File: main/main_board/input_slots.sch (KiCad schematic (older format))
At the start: 26 parts, among them J3 DEBUG, J7 SCKB, J8 SCKA, M1 microzed, U14 74LVC541A, U15 FIN1047, U16 FIN1047, U17 FIN1047, U5 DS90LV048, X1 microzed

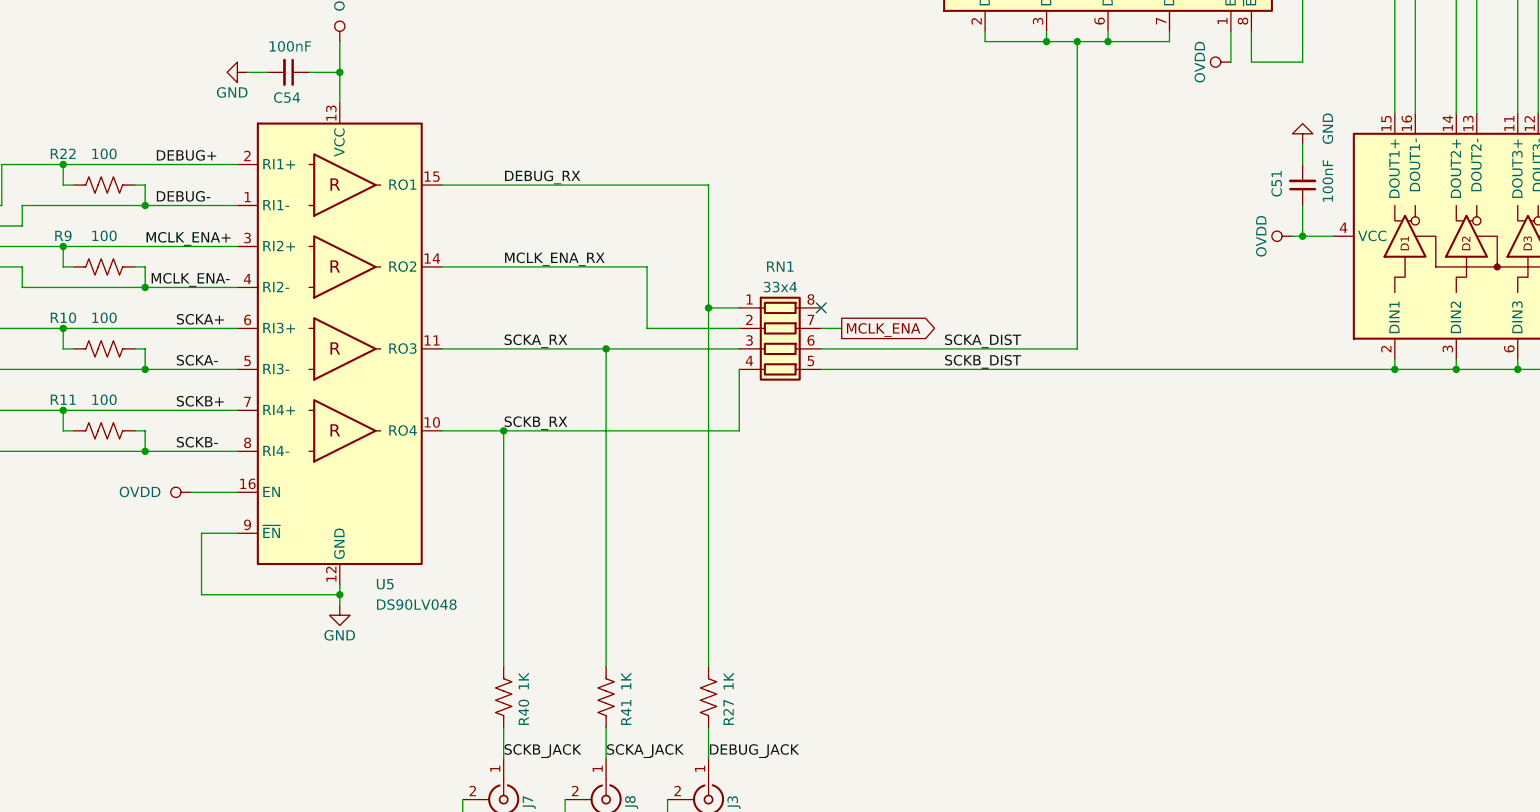
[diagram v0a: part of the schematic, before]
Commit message: Main board is now fully routed and passing DRC. Minor changes related to pin remapping. I2C and one-wire pullups are to OVDD 3.3V, not VCCIO 2.5V. Changes to supply decoupling and VREF- net in reference.sch, suggested by routing.
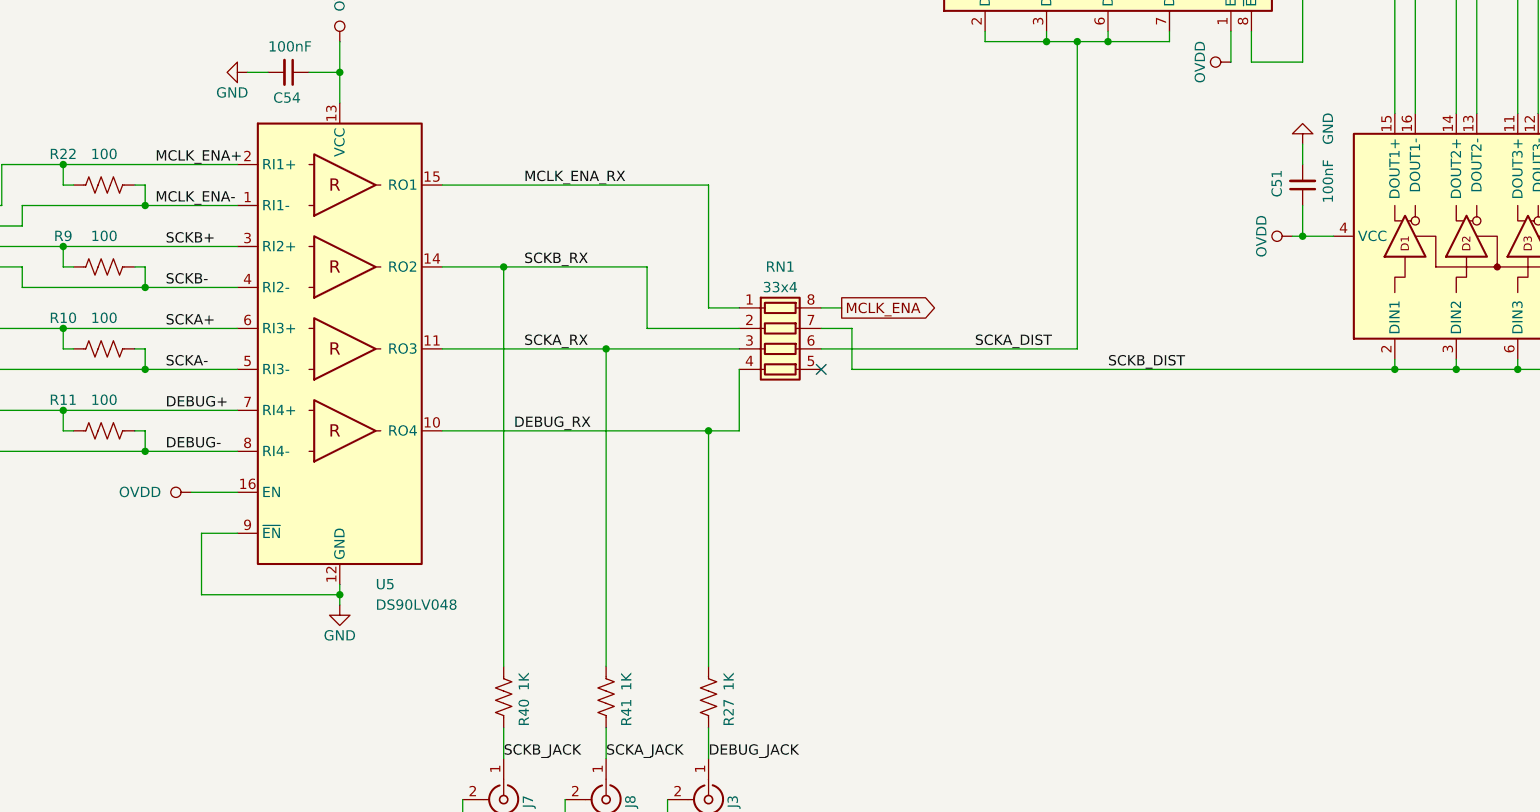
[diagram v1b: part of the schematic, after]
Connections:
- wire segments 333 -> 336
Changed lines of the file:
@@
 	8300 11950 8300 11650
 Wire Wire Line
-	8300 11650 7300 11650
+	8300 11650 7600 11650
 Wire Wire Line
 	8600 11850 8600 11250
 Wire Wire Line
 	8600 11250 7300 11250
-Text GLabel 9250 11950 2    50   Output ~ 0
+Text GLabel 9250 11850 2    50   Output ~ 0
 MCLK_ENA
 Wire Wire Line
-	9250 11950 9150 11950
-Wire Wire Line
-	7600 13600 7600 12450
+	9250 11850 9150 11850
 Wire Wire Line
 	8100 13600 8100 12050
@@
 Wire Wire Line
 	10400 10550 10400 12050
-Wire Wire Line
-	9150 12050 10400 12050
-Wire Wire Line
-	9150 12150 11950 12150
-Connection ~ 11950 12150
 Wire Wire Line
 	4400 11550 5450 11550
@@
 Wire Wire Line
 	2600 11550 2700 11550
-NoConn ~ 9150 11850
 NoConn ~ 6650 6300
 Wire Wire Line
@@
 Wire Wire Line
 	8900 8000 15850 8000
-Text Label 5850 11550 0    50   ~ 0
-MCLK_ENA+
-Text Label 5875 11750 0    50   ~ 0
-MCLK_ENA-
-Text Label 6000 11950 0    50   ~ 0
-SCKA+
-Text Label 6000 12150 0    50   ~ 0
-SCKA-
-Text Label 6000 12350 0    50   ~ 0
-SCKB+
-Text Label 6000 12550 0    50   ~ 0
-SCKB-
-Text Label 9750 12050 0    50   ~ 0
+Text Label 9900 12050 0    50   ~ 0
 SCKA_DIST
-Text Label 9750 12150 0    50   ~ 0
-SCKB_DIST
 $Comp
 L microzed:microzed M1
@@
 Wire Wire Line
 	5500 8500 5500 8600
-Text Label 7600 12050 0    50   ~ 0
+Text Label 7700 12050 0    50   ~ 0
 SCKA_RX
-Text Label 7600 12450 0    50   ~ 0
+Text Label 7700 11650 0    50   ~ 0
 SCKB_RX
-Text Label 7600 11650 0    50   ~ 0
+Text Label 7700 11250 0    50   ~ 0
 MCLK_ENA_RX
-Text Label 7600 11250 0    50   ~ 0
+Text Label 7650 12450 0    50   ~ 0
 DEBUG_RX
 Wire Wire Line
@@
 Wire Wire Line
 	8300 11950 8750 11950
-Wire Wire Line
-	7600 12450 7300 12450
 Connection ~ 8100 12050
 Wire Wire Line
-	8100 12050 7300 12050
-Connection ~ 8600 11850
-Wire Wire Line
 	8100 12050 8750 12050
 Wire Wire Line
 	8600 11850 8750 11850
 Wire Wire Line
-	8600 11850 8600 13600
-Wire Wire Line
-	7600 12450 8750 12450
-Wire Wire Line
 	8750 12450 8750 12150
-Connection ~ 7600 12450
-Text Label 5900 11150 0    50   ~ 0
-DEBUG+
-Text Label 5900 11350 0    50   ~ 0
-DEBUG-
 Wire Wire Line
 	5250 11350 5850 11350
-Connection ~ 5450 11550
-Connection ~ 5850 11750
-Wire Wire Line
-	5450 11550 6300 11550
-Wire Wire Line
-	5850 11750 6300 11750
-Connection ~ 5450 11950
-Connection ~ 5850 12150
-Wire Wire Line
-	5450 11950 6300 11950
-Wire Wire Line
-	5850 12150 6300 12150
-Connection ~ 5450 12350
-Connection ~ 5850 12550
-Wire Wire Line
-	5450 12350 6300 12350
-Wire Wire Line
-	5850 12550 6300 12550
 Wire Wire Line
 	4400 11150 4550 11150
@@
 Wire Wire Line
 	5850 11250 5850 11350
-Connection ~ 5450 11150
-Wire Wire Line
-	5450 11150 6300 11150
-Connection ~ 5850 11350
-Wire Wire Line
-	5850 11350 6300 11350
 Text GLabel 15700 3550 0    50   Input ~ 0
 IN1_CARDSEL
@@
 Wire Wire Line
 	8900 8000 8900 8300
+Connection ~ 5850 11350
+Wire Wire Line
+	5850 11350 6300 11350
+Connection ~ 5450 11150
+Wire Wire Line
+	5450 11150 6300 11150
+Connection ~ 5850 12550
+Wire Wire Line
+	5850 12550 6300 12550
+Connection ~ 5450 12350
+Wire Wire Line
+	5450 12350 6300 12350
+Connection ~ 5850 12150
+Wire Wire Line
+	5850 12150 6300 12150
+Connection ~ 5450 11950
+Wire Wire Line
+	5450 11950 6300 11950
+Connection ~ 5850 11750
+Wire Wire Line
+	5850 11750 6300 11750
+Connection ~ 5450 11550
+Wire Wire Line
+	5450 11550 6300 11550
+Text Label 5950 12350 0    50   ~ 0
+DEBUG+
+Text Label 5950 12550 0    50   ~ 0
+DEBUG-
+Text Label 5950 11950 0    50   ~ 0
+SCKA+
+Text Label 5950 12150 0    50   ~ 0
+SCKA-
+Text Label 5950 11550 0    50   ~ 0
+SCKB+
+Text Label 5950 11750 0    50   ~ 0
+SCKB-
+Text Label 5900 11150 0    50   ~ 0
+MCLK_ENA+
+Text Label 5900 11350 0    50   ~ 0
+MCLK_ENA-
+Wire Wire Line
+	8600 13600 8600 12450
+Wire Wire Line
+	7300 12450 8600 12450
+Connection ~ 8600 12450
+Wire Wire Line
+	8600 12450 8750 12450
+Connection ~ 7600 11650
+Wire Wire Line
+	7600 11650 7300 11650
+Wire Wire Line
+	7300 12050 8100 12050
+Wire Wire Line
+	7600 11650 7600 13600
+Text Label 10550 12150 0    50   ~ 0
+SCKB_DIST
+Wire Wire Line
+	9300 12150 11950 12150
+Connection ~ 11950 12150
+Wire Wire Line
+	9300 11950 9300 12150
+Wire Wire Line
+	9150 11950 9300 11950
+Wire Wire Line
+	9150 12050 10400 12050
+NoConn ~ 9150 12150
 $EndSCHEMATC

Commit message: Added testpoints, debug IO port, LEDs, and clock output jack.
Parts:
- removed M1: microzed, main_board:Microzed, symbol microzed:microzed
- removed unit 3 of X1
- added M1: microzed, main_board:Microzed, symbol microzed:microzed
- J3, J7, J8: DK line (none) -> 35
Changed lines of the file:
@@
 F 2 "Connector_Coaxial:MMCX_Molex_73415-1471_Vertical" H 8100 14250 50  0001 C CNN
 F 3 "https://www.molex.com/pdm_docs/sd/734151471_sd.pdf" H 8100 14250 50  0001 C CNN
-F 4 "" H 8100 14250 50  0001 C CNN "DK line"
+F 4 "35" H 8100 14250 50  0001 C CNN "DK line"
 F 5 "CONN MMCX JACK STR 50 OHM PCB" H 8100 14250 50  0001 C CNN "Description"
 F 6 "WM5557-ND" H 8100 14250 50  0001 C CNN "Digikey"
@@
 F 2 "Connector_Coaxial:MMCX_Molex_73415-1471_Vertical" H 7600 14250 50  0001 C CNN
 F 3 "https://www.molex.com/pdm_docs/sd/734151471_sd.pdf" H 7600 14250 50  0001 C CNN
-F 4 "" H 7600 14250 50  0001 C CNN "DK line"
+F 4 "35" H 7600 14250 50  0001 C CNN "DK line"
 F 5 "CONN MMCX JACK STR 50 OHM PCB" H 7600 14250 50  0001 C CNN "Description"
 F 6 "WM5557-ND" H 7600 14250 50  0001 C CNN "Digikey"
@@
 Wire Wire Line
 	4600 12550 5850 12550
+Wire Wire Line
+	17000 1850 17800 1850
+Wire Wire Line
+	17800 1850 17800 1950
+Wire Wire Line
+	17000 1950 17700 1950
+Wire Wire Line
+	17700 1950 17700 2050
+Wire Wire Line
+	17700 2050 17800 2050
+Wire Wire Line
+	17000 2100 17650 2100
+Wire Wire Line
+	17650 2100 17650 2150
+Wire Wire Line
+	17650 2150 17800 2150
+Wire Wire Line
+	17000 2200 17600 2200
+Wire Wire Line
+	17600 2200 17600 2250
+Wire Wire Line
+	17600 2250 17800 2250
+Wire Wire Line
+	17000 2350 17800 2350
+Wire Wire Line
+	17000 2450 17800 2450
+Wire Wire Line
+	17000 2600 17600 2600
+Wire Wire Line
+	17600 2600 17600 2550
+Wire Wire Line
+	17600 2550 17800 2550
+Wire Wire Line
+	17000 2700 17700 2700
+Wire Wire Line
+	17700 2700 17700 2650
+Wire Wire Line
+	17700 2650 17800 2650
 $Comp
 L microzed:microzed X1
-U 3 1 5F0A97DA
-P 17800 1950
-AR Path="/5F0A97DA" Ref="X1"  Part="2"
-AR Path="/5E525FFE/5F0A97DA" Ref="M1"  Part="3"
-F 0 "M1" H 18000 2200 60  0000 L CNN
-F 1 "microzed" H 18000 2100 60  0000 L CNN
-F 2 "main_board:Microzed" H 18000 2000 60  0001 L CNN
-F 3 "" H 18000 1800 60  0001 L CNN
-	3    17800 1950
-	1    0    0    -1
-$EndComp
-Wire Wire Line
-	17000 1850 17800 1850
-Wire Wire Line
-	17800 1850 17800 1950
-Wire Wire Line
-	17000 1950 17700 1950
-Wire Wire Line
-	17700 1950 17700 2050
-Wire Wire Line
-	17700 2050 17800 2050
-Wire Wire Line
-	17000 2100 17650 2100
-Wire Wire Line
-	17650 2100 17650 2150
-Wire Wire Line
-	17650 2150 17800 2150
-Wire Wire Line
-	17000 2200 17600 2200
-Wire Wire Line
-	17600 2200 17600 2250
-Wire Wire Line
-	17600 2250 17800 2250
-Wire Wire Line
-	17000 2350 17800 2350
-Wire Wire Line
-	17000 2450 17800 2450
-Wire Wire Line
-	17000 2600 17600 2600
-Wire Wire Line
-	17600 2600 17600 2550
-Wire Wire Line
-	17600 2550 17800 2550
-Wire Wire Line
-	17000 2700 17700 2700
-Wire Wire Line
-	17700 2700 17700 2650
-Wire Wire Line
-	17700 2650 17800 2650
-$Comp
-L microzed:microzed X1
-U 4 1 5F159E9E
+U 5 1 5F159E9E
 P 17800 3600
 AR Path="/5F159E9E" Ref="X1"  Part="3"
-AR Path="/5E525FFE/5F159E9E" Ref="M1"  Part="4"
+AR Path="/5E525FFE/5F159E9E" Ref="M1"  Part="5"
 F 0 "M1" H 18000 3850 60  0000 L CNN
 F 1 "microzed" H 18000 3750 60  0000 L CNN
 F 2 "main_board:Microzed" H 18000 3650 60  0001 L CNN
 F 3 "" H 18000 3450 60  0001 L CNN
-	4    17800 3600
+	5    17800 3600
 	1    0    0    -1
 $EndComp
@@
 $Comp
 L microzed:microzed X1
-U 5 1 5F1854CB
+U 6 1 5F1854CB
 P 17800 5300
 AR Path="/5F1854CB" Ref="X1"  Part="4"
-AR Path="/5E525FFE/5F1854CB" Ref="M1"  Part="5"
+AR Path="/5E525FFE/5F1854CB" Ref="M1"  Part="6"
 F 0 "M1" H 18000 5550 60  0000 L CNN
 F 1 "microzed" H 18000 5450 60  0000 L CNN
 F 2 "main_board:Microzed" H 18000 5350 60  0001 L CNN
 F 3 "" H 18000 5150 60  0001 L CNN
-	5    17800 5300
+	6    17800 5300
 	1    0    0    -1
 $EndComp
@@
 $Comp
 L microzed:microzed X1
-U 6 1 5F209C7E
+U 7 1 5F209C7E
 P 17800 7050
 AR Path="/5F209C7E" Ref="X1"  Part="5"
-AR Path="/5E525FFE/5F209C7E" Ref="M1"  Part="6"
+AR Path="/5E525FFE/5F209C7E" Ref="M1"  Part="7"
 F 0 "M1" H 18000 7300 60  0000 L CNN
 F 1 "microzed" H 18000 7200 60  0000 L CNN
 F 2 "main_board:Microzed" H 18000 7100 60  0001 L CNN
 F 3 "" H 18000 6900 60  0001 L CNN
-	6    17800 7050
+	7    17800 7050
 	1    0    0    -1
 $EndComp
@@
 Text Label 9900 12050 0    50   ~ 0
 SCKA_DIST
-$Comp
-L microzed:microzed M1
-U 2 1 5F079106
-P 2700 11150
-F 0 "M1" H 2900 11400 60  0000 L CNN
-F 1 "microzed" H 2900 11300 60  0000 L CNN
-F 2 "main_board:Microzed" H 2900 11200 60  0001 L CNN
-F 3 "" H 2900 11000 60  0001 L CNN
-	2    2700 11150
-	1    0    0    -1
-$EndComp
 Wire Wire Line
 	4550 8200 4550 11150
@@
 F 2 "Connector_Coaxial:MMCX_Molex_73415-1471_Vertical" H 8600 14250 50  0001 C CNN
 F 3 "https://www.molex.com/pdm_docs/sd/734151471_sd.pdf" H 8600 14250 50  0001 C CNN
-F 4 "" H 8600 14250 50  0001 C CNN "DK line"
+F 4 "35" H 8600 14250 50  0001 C CNN "DK line"
 F 5 "CONN MMCX JACK STR 50 OHM PCB" H 8600 14250 50  0001 C CNN "Description"
 F 6 "WM5557-ND" H 8600 14250 50  0001 C CNN "Digikey"
@@
 Text GLabel 15700 3550 0    50   Input ~ 0
 IN1_CARDSEL
-Text GLabel 15700 5250 0    50   Input ~ 0
-IN2_CARDSEL
 Text GLabel 15700 7000 0    50   Input ~ 0
 IN3_CARDSEL
@@
 	9150 12050 10400 12050
 NoConn ~ 9150 12150
+$Comp
+L microzed:microzed M1
+U 4 1 5F1486B6
+P 17800 1950
+F 0 "M1" H 18000 2200 60  0000 L CNN
+F 1 "microzed" H 18000 2100 60  0000 L CNN
+F 2 "main_board:Microzed" H 18000 2000 60  0001 L CNN
+F 3 "" H 18000 1800 60  0001 L CNN
+	4    17800 1950
+	1    0    0    -1
+$EndComp
+$Comp
+L microzed:microzed M1
+U 3 1 5F151D97
+P 2700 11150
+F 0 "M1" H 2900 11400 60  0000 L CNN
+F 1 "microzed" H 2900 11300 60  0000 L CNN
+F 2 "main_board:Microzed" H 2900 11200 60  0001 L CNN
+F 3 "" H 2900 11000 60  0001 L CNN
+	3    2700 11150
+	1    0    0    -1
+$EndComp
+Text GLabel 15700 5250 0    50   Input ~ 0
+IN2_CARDSEL
 $EndSCHEMATC
